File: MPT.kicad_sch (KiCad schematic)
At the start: 6 parts, among them SW1 OS102011MA1QN1

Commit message: Rename to MultiPurpose Tracker (MPT)
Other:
- sheet BMS: file mpht_bms.kicad_sch -> mpt_bms.kicad_sch
- sheet MCU: file mpht_mcu.kicad_sch -> mpt_mcu.kicad_sch
- sheet USB: file mpht_usb.kicad_sch -> mpt_usb.kicad_sch
- title: MultiPurpose Habit Tracker (M.P.H.T.) -> MultiPurpose Tracker (M.P.T.)
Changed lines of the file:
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@@
 	(paper "A4")
 	(title_block
-		(title "MultiPurpose Habit Tracker (M.P.H.T.)")
+		(title "MultiPurpose Tracker (M.P.T.)")
 		(rev "1")
 		(company "Hochschule Luzern, Technik & Architektur")
@@
 		)
 		(instances
-			(project "MPHT"
+			(project "MPT"
 				(path "/328ebaa0-d01b-4b80-b614-bb0154e8d306"
 					(reference "R8")
@@
 		)
 		(instances
-			(project "MPHT"
+			(project "MPT"
 				(path "/328ebaa0-d01b-4b80-b614-bb0154e8d306"
 					(reference "#PWR06")
@@
 		)
 		(instances
-			(project "MPHT"
+			(project "MPT"
 				(path "/328ebaa0-d01b-4b80-b614-bb0154e8d306"
 					(reference "SW1")
@@
 		)
 		(instances
-			(project "MPHT"
+			(project "MPT"
 				(path "/328ebaa0-d01b-4b80-b614-bb0154e8d306"
 					(reference "R9")
@@
 		)
 		(instances
-			(project "MPHT"
+			(project "MPT"
 				(path "/328ebaa0-d01b-4b80-b614-bb0154e8d306"
 					(reference "#PWR043")
@@
 		)
 		(instances
-			(project "MPHT"
+			(project "MPT"
 				(path "/328ebaa0-d01b-4b80-b614-bb0154e8d306"
 					(reference "#PWR044")
@@
 		)
 		(instances
-			(project "MPHT"
+			(project "MPT"
 				(path "/328ebaa0-d01b-4b80-b614-bb0154e8d306"
 					(reference "R4")
@@
 		)
 		(instances
-			(project "MPHT"
+			(project "MPT"
 				(path "/328ebaa0-d01b-4b80-b614-bb0154e8d306"
 					(reference "R6")
@@
 		)
 		(instances
-			(project "MPHT"
+			(project "MPT"
 				(path "/328ebaa0-d01b-4b80-b614-bb0154e8d306"
 					(reference "#PWR05")
@@
 		)
 		(instances
-			(project "MPHT"
+			(project "MPT"
 				(path "/328ebaa0-d01b-4b80-b614-bb0154e8d306"
 					(reference "R5")
@@
 			)
 		)
-		(property "Sheetfile" "mpht_bms.kicad_sch"
+		(property "Sheetfile" "mpt_bms.kicad_sch"
 			(at 55.88 85.6746 0)
 			(show_name no)
@@
 		)
 		(instances
-			(project "MPHT"
+			(project "MPT"
 				(path "/328ebaa0-d01b-4b80-b614-bb0154e8d306"
 					(page "2")
@@
 			)
 		)
-		(property "Sheetfile" "mpht_mcu.kicad_sch"
+		(property "Sheetfile" "mpt_mcu.kicad_sch"
 			(at 113.03 93.2946 0)
 			(show_name no)
@@
 		)
 		(instances
-			(project "MPHT"
+			(project "MPT"
 				(path "/328ebaa0-d01b-4b80-b614-bb0154e8d306"
 					(page "3")
@@
 			)
 		)
-		(property "Sheetfile" "mpht_usb.kicad_sch"
+		(property "Sheetfile" "mpt_usb.kicad_sch"
 			(at 59.055 103.4546 0)
 			(show_name no)
@@
 		)
 		(instances
-			(project "MPHT"
+			(project "MPT"
 				(path "/328ebaa0-d01b-4b80-b614-bb0154e8d306"
 					(page "4")

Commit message: Add Text on PCB for reset and boot button
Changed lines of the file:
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@@
 		)
 	)
-	(label "Buck_En"
+	(label "BUCK_EN"
 		(at 43.18 82.55 0)
 		(effects
@@
 	)
 	(symbol
-		(lib_name "resistor/00.000.0000.0002_1")
 		(lib_id "db:resistor/00.000.0000.0002")
 		(at 223.52 74.93 0)
@@
 	)
 	(symbol
-		(lib_name "resistor/00.000.0000.0002_1")
 		(lib_id "db:resistor/00.000.0000.0002")
 		(at 181.61 105.41 0)

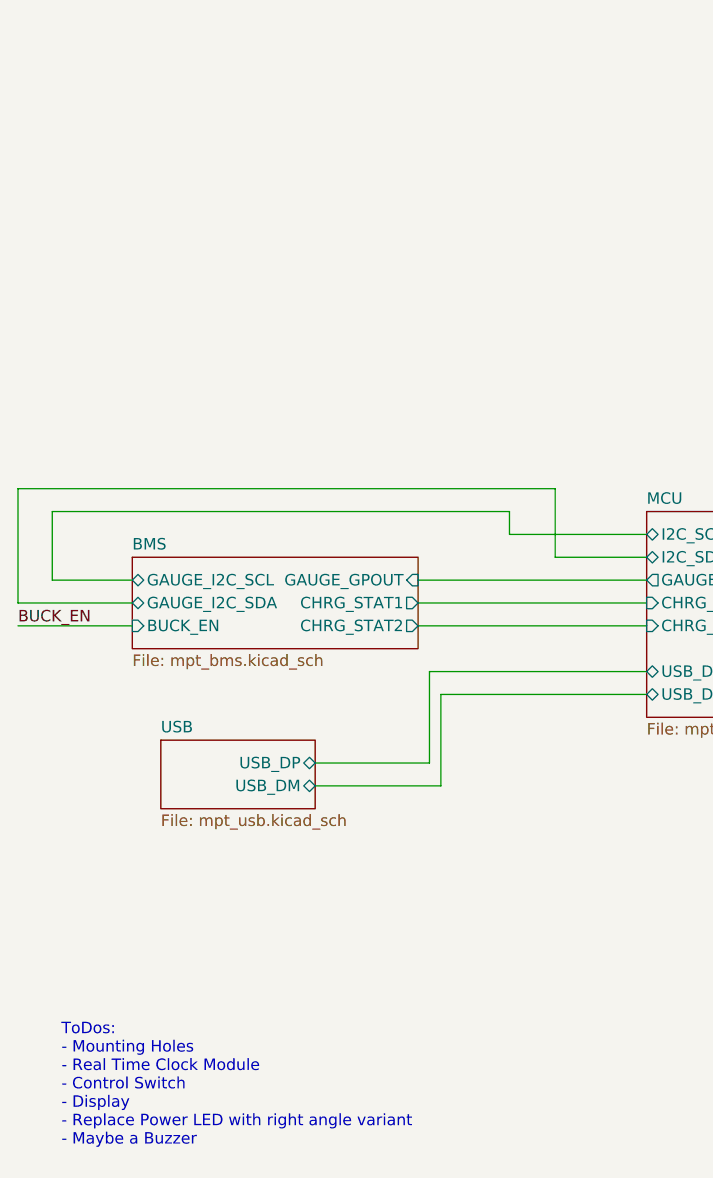
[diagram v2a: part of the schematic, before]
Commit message: Realt Time Clock document created
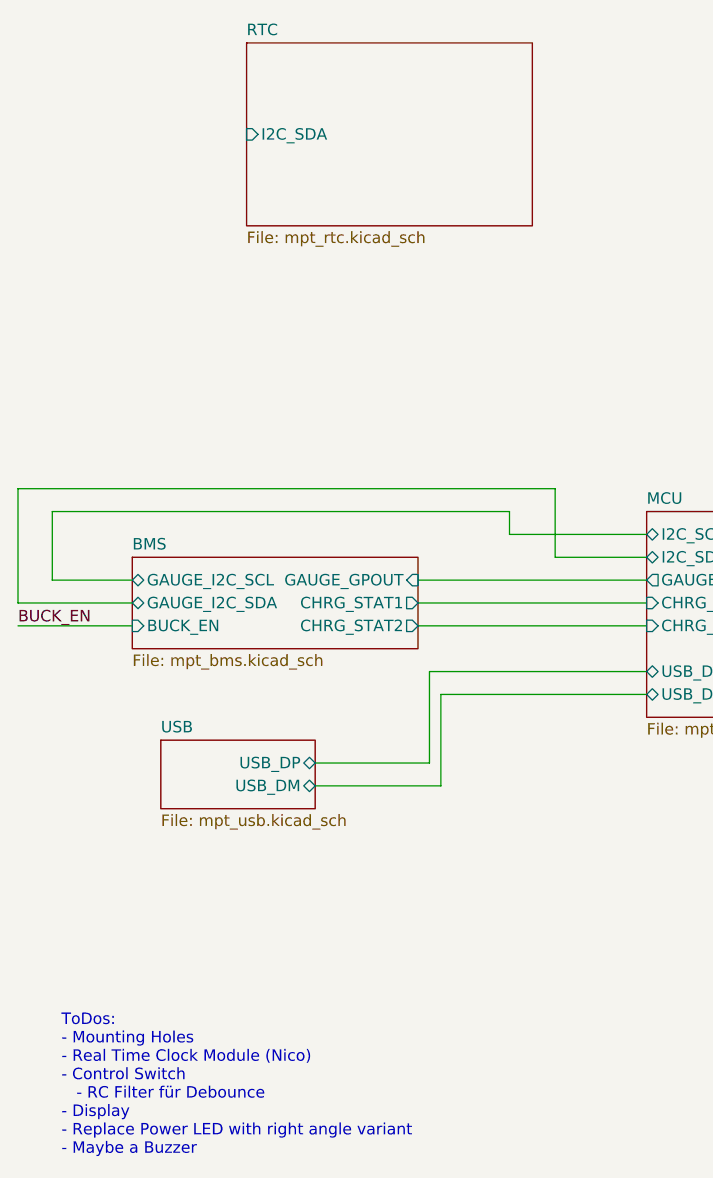
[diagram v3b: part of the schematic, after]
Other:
- added sheet RTC (mpt_rtc.kicad_sch)
- note added: "ToDos: - Mounting Holes - Real Time Clock Module (Nico) - Control Switch - RC Filter für Debounce - Display - Replace Power LED with right angle variant - Maybe a Buzzer"
- note removed: "ToDos: - Mounting Holes - Real Time Clock Module - Control Switch - Display - Replace Power LED with right angle variant - Maybe a Buzzer"
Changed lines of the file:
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@@
 		)
 	)
-	(text "ToDos:\n- Mounting Holes\n- Real Time Clock Module\n- Control Switch\n- Display\n- Replace Power LED with right angle variant\n- Maybe a Buzzer"
+	(text "ToDos:\n- Mounting Holes\n- Real Time Clock Module (Nico)\n- Control Switch\n   - RC Filter für Debounce\n- Display\n- Replace Power LED with right angle variant\n- Maybe a Buzzer"
 		(exclude_from_sim no)
 		(at 48.006 133.604 0)
@@
 				)
 			)
+		)
+	)
+	(sheet
+		(at 68.58 17.78)
+		(size 31.75 20.32)
+		(exclude_from_sim no)
+		(in_bom yes)
+		(on_board yes)
+		(dnp no)
+		(fields_autoplaced yes)
+		(stroke
+			(width 0.1524)
+			(type solid)
+		)
+		(fill
+			(color 0 0 0 0)
+		)
+		(property "Sheetname" "RTC"
+			(at 68.58 17.0684 0)
+			(show_name no)
+			(do_not_autoplace no)
+			(effects
+				(font
+					(size 1.27 1.27)
+				)
+				(justify left bottom)
+			)
+		)
+		(property "Sheetfile" "mpt_rtc.kicad_sch"
+			(at 68.58 38.6846 0)
+			(show_name no)
+			(do_not_autoplace no)
+			(effects
+				(font
+					(size 1.27 1.27)
+				)
+				(justify left top)
+			)
+		)
+		(pin "I2C_SDA" input
+			(at 68.58 27.94 180)
+			(effects
+				(font
+					(size 1.27 1.27)
+				)
+				(justify left)
+			)
+		)
+		(instances
+			(project "MPT"
+				(path "/328ebaa0-d01b-4b80-b614-bb0154e8d306"
+					(page "5")
+				)
+			)

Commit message: Added Display
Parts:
- R3: renamed from R5; symbol db:resistor/00.000.0000.0001 -> db:resistor_0603/00.000.0000.0001
- R5: renamed from R6; symbol db:resistor/00.018.0009.0006 -> db:resistor_0603/00.018.0009.0046; Modified 2026-02-11 09:36:06 -> 2026-10-07 14:47:41; Rating 100mW, 1% -> 125mW, 1%; Remarks (none) -> Autogenerated
- renumbered R9 to R1, R4 to R2, R8 to R4
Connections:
- net GND: now also SW1.4 (SH)
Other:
- added sheet Display (mpt_display.kicad_sch)
- sheet MCU ports: added DISP_RESET, DISP_RS, SPI2_SDA; removed SPI2_SDA0, SPI2_SDA1, SPI2_SDA2, SPI2_SDA3
- note added: "Buck Shutdown: The Buckconverter is shutdown. Only the BMS and the RTC get power from the batteries. MCU Shutdown: The MCU get the signal to shutdown and goes into deepsleep."
- note added: "Select On/Off Type: - Buck Shutdown: R5 10k, R3 0 - MCU Shutdown: R1 10k, R4 10k, R2 0"
- note added: "ToDos: - Mounting Holes - Real Time Clock Module (Nico) - Control Switch (Nico) - RC Filter für Debounce - Backlight Mosfet - Maybe a Buzzer - Testpoints"
- note removed: "Select On/Off Type: - Buck Shutdown: R6 10k, R5 0 - MCU Shutdown: R8 10k, R4 0, R9 0"
- note removed: "ToDos: - Mounting Holes - Real Time Clock Module (Nico) - Control Switch - RC Filter für Debounce - Display - Replace Power LED with right angle variant - Maybe a Buzzer"
- moved on the sheet: R1, R2, R3, R4, R5

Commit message: Added Sheets for optional Buzzer and User Buttons
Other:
- added sheet Maybe Buzzer (mpt_buzzer.kicad_sch)
- added sheet User Buttons (mpt_user_buttons.kicad_sch)
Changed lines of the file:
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@@
 	)
 	(sheet
-		(at 68.58 17.78)
+		(at 54.61 148.59)
 		(size 31.75 20.32)
 		(exclude_from_sim no)
@@
 		)
 		(property "Sheetname" "RTC"
-			(at 68.58 17.0684 0)
+			(at 54.61 147.8784 0)
 			(show_name no)
 			(do_not_autoplace no)
@@
 		)
 		(property "Sheetfile" "mpt_rtc.kicad_sch"
-			(at 68.58 38.6846 0)
+			(at 54.61 169.4946 0)
 			(show_name no)
 			(do_not_autoplace no)
@@
 		)
 		(pin "I2C_SDA" input
-			(at 68.58 27.94 180)
+			(at 54.61 158.75 180)
 			(effects
 				(font
@@
 				(path "/328ebaa0-d01b-4b80-b614-bb0154e8d306"
 					(page "5")
+				)
+			)
+		)
+	)
+	(sheet
+		(at 10.16 11.43)
+		(size 30.48 20.32)
+		(exclude_from_sim no)
+		(in_bom yes)
+		(on_board yes)
+		(dnp no)
+		(fields_autoplaced yes)
+		(stroke
+			(width 0.1524)
+			(type solid)
+		)
+		(fill
+			(color 0 0 0 0)
+		)
+		(property "Sheetname" "Maybe Buzzer"
+			(at 10.16 10.7184 0)
+			(show_name no)
+			(do_not_autoplace no)
+			(effects
+				(font
+					(size 1.27 1.27)
+				)
+				(justify left bottom)
+			)
+		)
+		(property "Sheetfile" "mpt_buzzer.kicad_sch"
+			(at 10.16 32.3346 0)
+			(show_name no)
+			(do_not_autoplace no)
+			(effects
+				(font
+					(size 1.27 1.27)
+				)
+				(justify left top)
+			)
+		)
+		(instances
+			(project "MPT"
+				(path "/328ebaa0-d01b-4b80-b614-bb0154e8d306"
+					(page "8")
 				)
 			)
@@
 				)
 			)
+		)
+	)
+	(sheet
+		(at 96.52 152.4)
+		(size 25.4 21.59)
+		(exclude_from_sim no)
+		(in_bom yes)
+		(on_board yes)
+		(dnp no)
+		(fields_autoplaced yes)
+		(stroke
+			(width 0.1524)
+			(type solid)
+		)
+		(fill
+			(color 0 0 0 0)
+		)
+		(property "Sheetname" "User Buttons"
+			(at 96.52 151.6884 0)
+			(show_name no)
+			(do_not_autoplace no)
+			(effects
+				(font
+					(size 1.27 1.27)
+				)
+				(justify left bottom)
+			)
+		)
+		(property "Sheetfile" "mpt_user_buttons.kicad_sch"
+			(at 96.52 174.5746 0)
+			(show_name no)
+			(do_not_autoplace no)
+			(effects
+				(font
+					(size 1.27 1.27)
+				)
+				(justify left top)
+			)
+		)
+		(instances
+			(project "MPT"
+				(path "/328ebaa0-d01b-4b80-b614-bb0154e8d306"
+					(page "7")
+				)
+			)

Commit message: Work in Progress of RTC Added Sheet Titles
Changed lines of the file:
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@@
 			)
 		)
-		(pin "I2C_SDA" input
+		(pin "I2C_SDA" bidirectional
 			(at 54.61 158.75 180)
 			(effects
